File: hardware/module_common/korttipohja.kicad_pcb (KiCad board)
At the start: 2 copper layers, 100 x 100 mm, 5 parts, among them J1 RJ45_LED, U1 WAVGAT_CAN

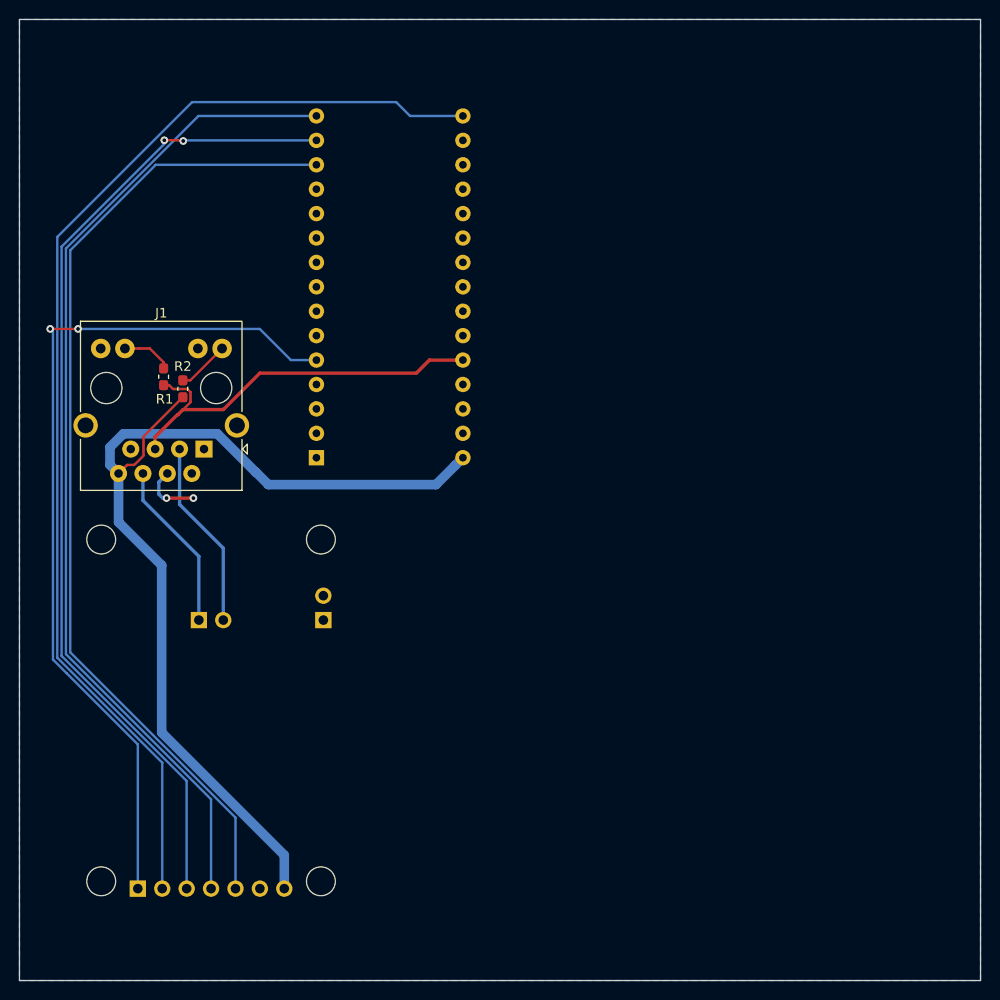
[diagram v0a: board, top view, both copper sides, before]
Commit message: Finish first iteration of module common backplane
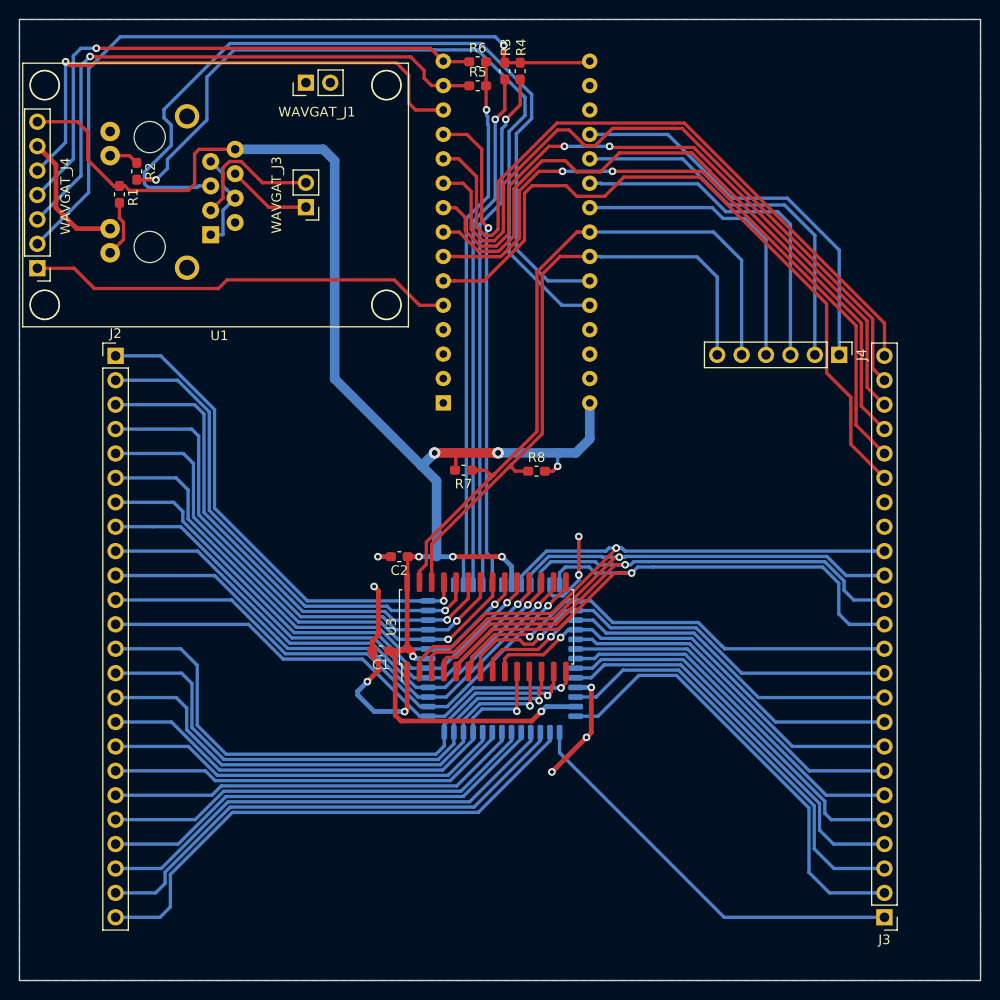
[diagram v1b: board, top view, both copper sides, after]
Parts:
- added C1: 0.1uF, Capacitor_SMD:C_0603_1608Metric_Pad1.05x0.95mm_HandSolder, F.Cu at (107.6, 115.7)
- added C2: 0.1uF, Capacitor_SMD:C_0603_1608Metric_Pad1.05x0.95mm_HandSolder, F.Cu at (109.5, 105.9)
- added J2: Conn_01x24_Female, Connector_PinHeader_2.54mm:PinHeader_1x24_P2.54mm_Vertical, F.Cu at (80.0, 85.0)
- added J3: Conn_01x24_Female, Connector_PinHeader_2.54mm:PinHeader_1x24_P2.54mm_Vertical, F.Cu at (160.0, 143.4)
- added J4: Conn_01x06_Male, Connector_PinHeader_2.54mm:PinHeader_1x06_P2.54mm_Vertical, F.Cu at (155.3, 84.9)
- added R3: 0R, Resistor_SMD:R_0603_1608Metric_Pad1.05x0.95mm_HandSolder, F.Cu at (120.5, 55.4)
- added R4: 0R, Resistor_SMD:R_0603_1608Metric_Pad1.05x0.95mm_HandSolder, F.Cu at (122.1, 55.4)
- added R5: 0R, Resistor_SMD:R_0603_1608Metric_Pad1.05x0.95mm_HandSolder, F.Cu at (117.7, 56.9)
- added R6: 0R, Resistor_SMD:R_0603_1608Metric_Pad1.05x0.95mm_HandSolder, F.Cu at (117.7, 54.4)
- added R7: 4K7, Resistor_SMD:R_0603_1608Metric_Pad1.05x0.95mm_HandSolder, F.Cu at (116.2, 96.9)
- added R8: 4K7, Resistor_SMD:R_0603_1608Metric_Pad1.05x0.95mm_HandSolder, F.Cu at (123.8, 97.0)
- added U2: HT1632C-52LQFP, Package_QFP:LQFP-52_14x14mm_P1mm, B.Cu at (120.2, 116.5)
- added U3: HT16K33, Package_SO:SOIC-28W_7.5x17.9mm_P1.27mm, F.Cu at (118.6, 113.2)
- J1: moved to B.Cu
- U1: moved to F.Cu
- moved U1 84.5 mm to (80.5, 51.5), turned to 0 degrees
- moved J1 22.3 mm to (89.9, 72.4), turned to 90 degrees
- moved R2 21.6 mm to (82.2, 65.8)
- moved R1 21.3 mm to (80.4, 68.2), turned to 270 degrees
- moved A1 14.4 mm to (114.1, 89.9)
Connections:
- net Net-(A1-Pad14) renamed MOSI
- net Net-(A1-Pad15) renamed MISO
- net Net-(A1-Pad16) renamed SCK
- A1 pad 10: (no net) -> D7
- A1 pad 11: (no net) -> D8
- A1 pad 12: (no net) -> CS_LED
- A1 pad 19: (no net) -> Net-(A1-Pad19)
- A1 pad 20: (no net) -> Net-(A1-Pad20)
- A1 pad 21: (no net) -> Net-(A1-Pad21)
- A1 pad 22: (no net) -> Net-(A1-Pad22)
- A1 pad 23: (no net) -> SDA
- A1 pad 24: (no net) -> SCL
- A1 pad 25: (no net) -> MODULE_ENABLE
- A1 pad 6: (no net) -> D3
- A1 pad 7: (no net) -> D4
- A1 pad 8: (no net) -> D5
- A1 pad 9: (no net) -> D6
- J1 pad 5: STATUS_GOOD -> MODULE_ENABLE
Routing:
- net MODULE_ENABLE: track 0.00 -> 85.4 mm
- net SDA: track 0.00 -> 74.7 mm
- net D3: track 0.00 -> 74.2 mm
- net D7: track 0.00 -> 73.7 mm
- net D8: track 0.00 -> 72.0 mm
- net D5: track 0.00 -> 71.8 mm
- net D6: track 0.00 -> 70.7 mm, vias 0 -> 2
- net D4: track 0.00 -> 70.7 mm, vias 0 -> 2
- net SCL: track 0.00 -> 67.7 mm
- net COM0: track 0.00 -> 66.5 mm, vias 0 -> 1
- net VCC: track 105.2 -> 171.4 mm, vias 0 -> 8
- net COM1: track 0.00 -> 65.0 mm, vias 0 -> 1
- net COM2: track 0.00 -> 64.2 mm, vias 0 -> 1
- net GND: track 6.29 -> 69.7 mm, vias 2 -> 9
- net COM3: track 0.00 -> 63.1 mm, vias 0 -> 1
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
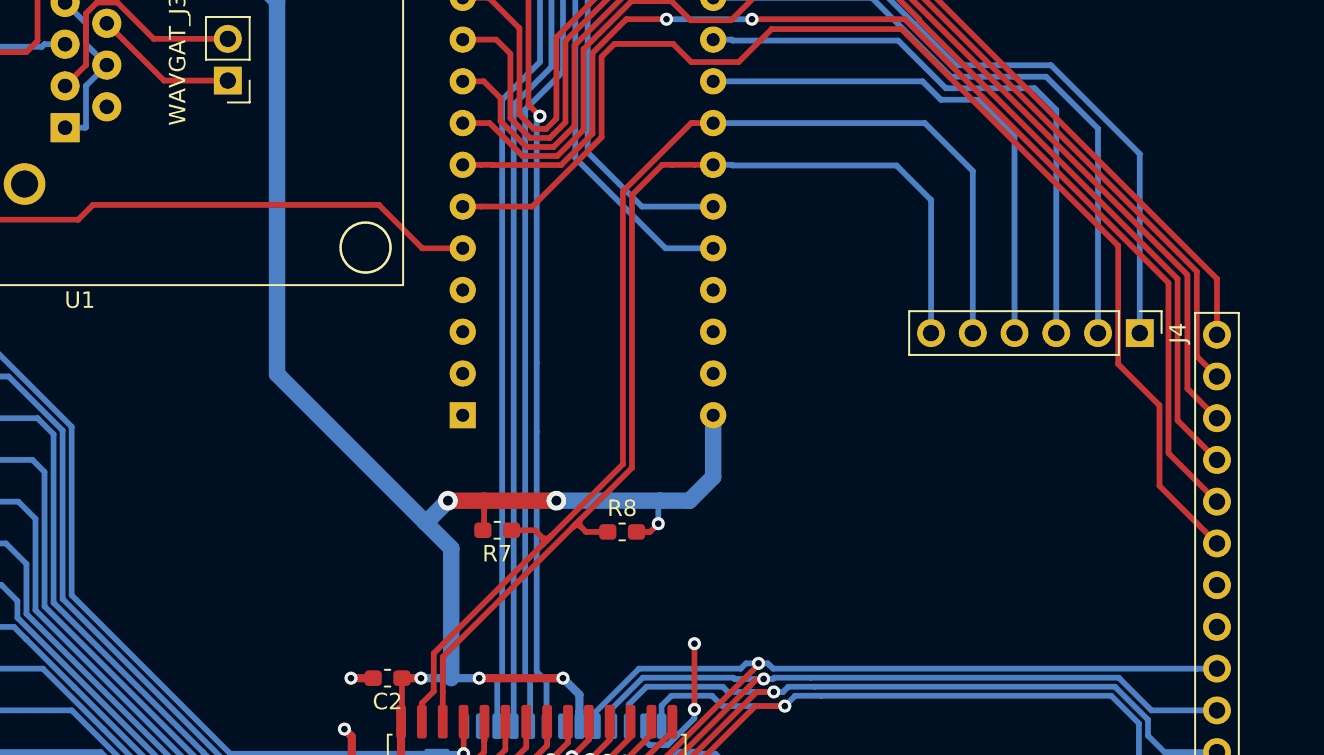
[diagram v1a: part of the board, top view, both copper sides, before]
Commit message: Add +5V and +12V to module funcitonal PCB.
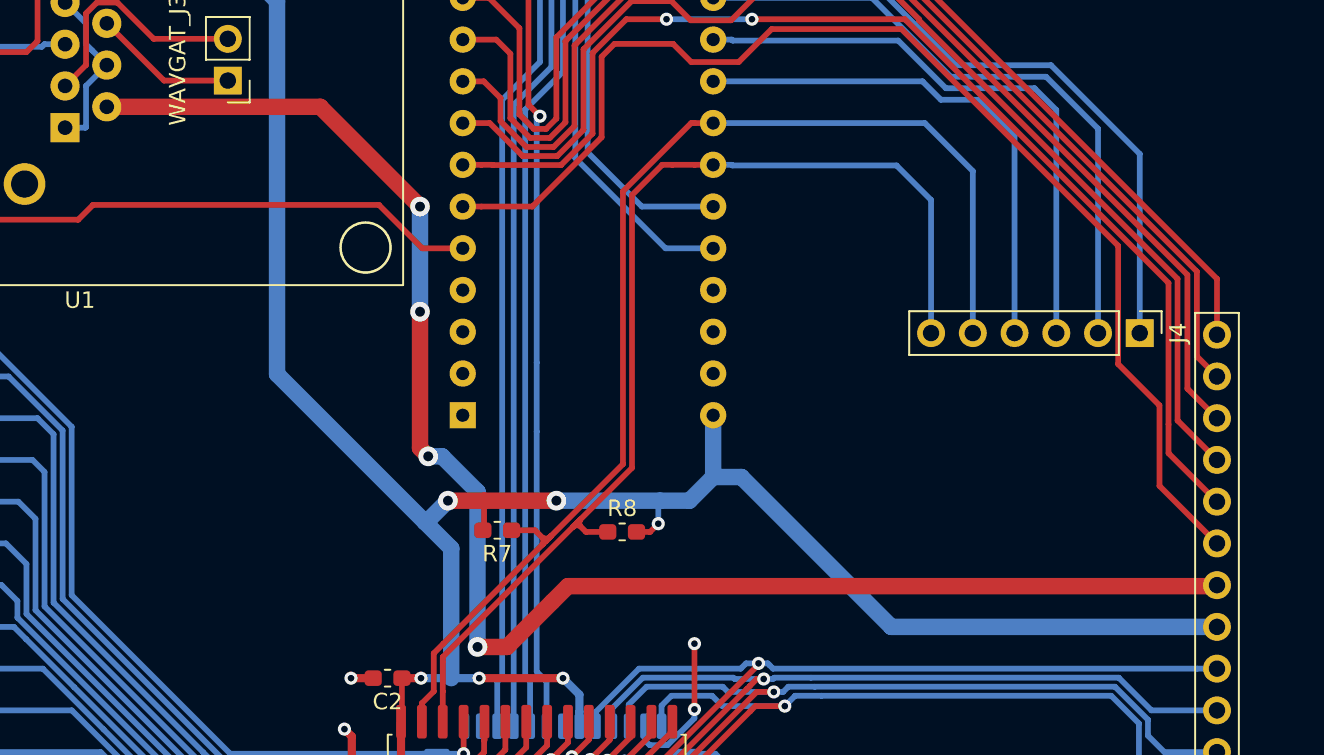
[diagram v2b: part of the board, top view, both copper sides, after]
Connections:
- J1 pad 2: (no net) -> +12V
- J3 pad 17: (no net) -> VCC
- J3 pad 18: (no net) -> +12V
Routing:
- net +12V: track 0.00 -> 96.9 mm, vias 0 -> 4
- net VCC: track 171.4 -> 205.8 mm
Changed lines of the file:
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@@
     (thickness 1.6)
     (drawings 4)
-    (tracks 864)
+    (tracks 884)
     (zones 0)
     (modules 18)
-    (nets 70)
+    (nets 71)
   )
   (page A4)
@@
   )
   (setup
-    (last_trace_width 0.5)
+    (last_trace_width 1)
     (user_trace_width 0.35)
     (user_trace_width 0.5)
@@
   (net 68 D7)
   (net 69 D8)
+  (net 70 +12V)
   (net_class Default "This is the default net class."
     (clearance 0.2)
@@
     (uvia_dia 0.3)
     (uvia_drill 0.1)
+    (add_net +12V)
     (add_net COM0)
     (add_net COM1)
@@
     (pad 1 thru_hole rect (at 0 0 90) (size 1.778 1.778) (drill 0.889) (layers *.Cu *.Mask)
       (net 1 GND))
-    (pad 2 thru_hole circle (at 1.27 2.54 90) (size 1.778 1.778) (drill 0.889) (layers *.Cu *.Mask))
+    (pad 2 thru_hole circle (at 1.27 2.54 90) (size 1.778 1.778) (drill 0.889) (layers *.Cu *.Mask)
+      (net 70 +12V))
     (pad 3 thru_hole circle (at 2.54 0 90) (size 1.778 1.778) (drill 0.889) (layers *.Cu *.Mask)
       (net 6 "Net-(J1-Pad3)"))
@@
     (pad 19 thru_hole oval (at 0 45.72 180) (size 1.7 1.7) (drill 1) (layers *.Cu *.Mask)
       (net 64 D3))
-    (pad 18 thru_hole oval (at 0 43.18 180) (size 1.7 1.7) (drill 1) (layers *.Cu *.Mask))
-    (pad 17 thru_hole oval (at 0 40.64 180) (size 1.7 1.7) (drill 1) (layers *.Cu *.Mask))
+    (pad 18 thru_hole oval (at 0 43.18 180) (size 1.7 1.7) (drill 1) (layers *.Cu *.Mask)
+      (net 70 +12V))
+    (pad 17 thru_hole oval (at 0 40.64 180) (size 1.7 1.7) (drill 1) (layers *.Cu *.Mask)
+      (net 5 VCC))
     (pad 16 thru_hole oval (at 0 38.1 180) (size 1.7 1.7) (drill 1) (layers *.Cu *.Mask)
       (net 45 COM0))
@@
   (segment (start 109.1 115.7) (end 109.5 115.7) (width 0.35) (layer F.Cu) (net 5))
   (segment (start 109.5 115.7) (end 110.375 115.7) (width 0.35) (layer F.Cu) (net 5))
+  (segment (start 129.34 93.66) (end 131.06 93.66) (width 1) (layer B.Cu) (net 5))
+  (segment (start 140.18 102.78) (end 160 102.78) (width 1) (layer B.Cu) (net 5))
+  (segment (start 131.06 93.66) (end 140.18 102.78) (width 1) (layer B.Cu) (net 5))
   (segment (start 91.833279 64.785999) (end 93.085999 64.785999) (width 0.35) (layer F.Cu) (net 6))
   (segment (start 91.175999 65.443279) (end 91.833279 64.785999) (width 0.35) (layer F.Cu) (net 6))
@@
   (segment (start 115.7 64.5) (end 114.1 64.5) (width 0.35) (layer F.Cu) (net 69))
   (segment (start 117.54999 66.34999) (end 115.7 64.5) (width 0.35) (layer F.Cu) (net 69))
+  (segment (start 115 104) (end 116.8 104) (width 1) (layer F.Cu) (net 70))
+  (segment (start 92.44 71.13) (end 105.43 71.13) (width 1) (layer F.Cu) (net 70))
+  (segment (start 111.5 91.9) (end 112 92.4) (width 1) (layer F.Cu) (net 70))
+  (segment (start 112.848528 92.4) (end 115 94.551472) (width 1) (layer B.Cu) (net 70))
+  (segment (start 112 92.4) (end 112.848528 92.4) (width 1) (layer B.Cu) (net 70))
+  (segment (start 105.43 71.13) (end 111.5 77.2) (width 1) (layer F.Cu) (net 70))
+  (segment (start 111.5 83.6) (end 111.5 91.9) (width 1) (layer F.Cu) (net 70))
+  (segment (start 116.8 104) (end 119.55 101.25) (width 1) (layer F.Cu) (net 70))
+  (segment (start 115 94.551472) (end 115 104) (width 1) (layer B.Cu) (net 70))
+  (via (at 111.5 77.2) (size 1.2) (drill 0.6) (layers F.Cu B.Cu) (net 70))
+  (segment (start 111.5 77.2) (end 111.5 83.6) (width 1) (layer B.Cu) (net 70))
+  (segment (start 119.55 101.25) (end 120.5 100.3) (width 1) (layer F.Cu) (net 70))
+  (via (at 111.5 83.6) (size 1.2) (drill 0.6) (layers F.Cu B.Cu) (net 70))
+  (via (at 115 104) (size 1.2) (drill 0.6) (layers F.Cu B.Cu) (net 70))
+  (via (at 112 92.4) (size 1.2) (drill 0.6) (layers F.Cu B.Cu) (net 70))
+  (segment (start 159.94 100.3) (end 160 100.24) (width 1) (layer F.Cu) (net 70))
+  (segment (start 120.5 100.3) (end 159.94 100.3) (width 1) (layer F.Cu) (net 70))
   (zone (net 1) (net_name GND) (layer B.Cu) (hatch edge 0.508)
     (connect_pads (clearance 0.508))

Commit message: Add FETs for increased current control.
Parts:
- added Q1: Q_NMOS_GSD, Package_TO_SOT_SMD:SOT-23, B.Cu at (154.9, 88.9)
- added Q2: Q_NMOS_GSD, Package_TO_SOT_SMD:SOT-23, B.Cu at (151.4, 90.2)
- added Q3: Q_NMOS_GSD, Package_TO_SOT_SMD:SOT-23, B.Cu at (147.9, 91.6)
- added Q4: Q_NMOS_GSD, Package_TO_SOT_SMD:SOT-23, B.Cu at (144.4, 88.8)
- added Q5: Q_NMOS_GSD, Package_TO_SOT_SMD:SOT-23, B.Cu at (140.9, 90.2)
- added Q6: Q_NMOS_GSD, Package_TO_SOT_SMD:SOT-23, B.Cu at (137.4, 91.5)
- added R10: 0R, Resistor_SMD:R_0603_1608Metric_Pad1.05x0.95mm_HandSolder, B.Cu at (152.7, 81.8)
- added R11: 0R, Resistor_SMD:R_0603_1608Metric_Pad1.05x0.95mm_HandSolder, B.Cu at (150.2, 81.8)
- added R12: 0R, Resistor_SMD:R_0603_1608Metric_Pad1.05x0.95mm_HandSolder, B.Cu at (147.7, 81.8)
- added R13: 0R, Resistor_SMD:R_0603_1608Metric_Pad1.05x0.95mm_HandSolder, B.Cu at (145.2, 81.8)
- added R14: 0R, Resistor_SMD:R_0603_1608Metric_Pad1.05x0.95mm_HandSolder, B.Cu at (142.6, 81.8)
- added R16: 0R, Resistor_SMD:R_0603_1608Metric_Pad1.05x0.95mm_HandSolder, B.Cu at (143.8, 76.5)
- added R17: 0R, Resistor_SMD:R_0603_1608Metric_Pad1.05x0.95mm_HandSolder, B.Cu at (140.6, 79.3)
- added R9: 0R, Resistor_SMD:R_0603_1608Metric_Pad1.05x0.95mm_HandSolder, B.Cu at (155.3, 81.8)
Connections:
- J4 pad 1: Net-(A1-Pad19) -> Net-(J4-Pad1)
- J4 pad 2: Net-(A1-Pad20) -> Net-(J4-Pad2)
- J4 pad 3: Net-(A1-Pad21) -> Net-(J4-Pad3)
- J4 pad 4: Net-(A1-Pad22) -> Net-(J4-Pad4)
- J4 pad 5: SDA -> Net-(J4-Pad5)
- J4 pad 6: SCL -> Net-(J4-Pad6)
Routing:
- net GND: track 69.7 -> 135.6 mm, vias 9 -> 17
- net Net-(A1-Pad19): track 41.8 -> 103.9 mm, vias 0 -> 4
- net Net-(A1-Pad20): track 39.2 -> 91.6 mm, vias 0 -> 4
- net Net-(A1-Pad21): track 36.2 -> 77.1 mm, vias 0 -> 2
- net Net-(A1-Pad22): track 31.7 -> 68.5 mm, vias 0 -> 2
- net Net-(Q5-Pad1): track 0.00 -> 30.7 mm, vias 0 -> 2
- net Net-(Q6-Pad1): track 0.00 -> 15.8 mm
- net Net-(J4-Pad6): track 0.00 -> 11.8 mm
- net Net-(J4-Pad3): track 0.00 -> 9.52 mm
- net Net-(J4-Pad5): track 0.00 -> 9.29 mm
- net Net-(J4-Pad2): track 0.00 -> 8.14 mm
- net Net-(J4-Pad4): track 0.00 -> 7.09 mm
- net Net-(J4-Pad1): track 0.00 -> 6.42 mm
- net SCL: track 67.7 -> 64.8 mm
- net SDA: track 74.7 -> 73.2 mm
